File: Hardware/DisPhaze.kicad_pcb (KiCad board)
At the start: 2 copper layers, 71 x 24.1 mm, 13 parts, among them J1 Conn_01x27, J2 Conn_01x27, J3 Conn_01x04_Male, U1 STM32F405RGTx, Y1 Crystal

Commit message: Start PCB layout
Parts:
- added C10: 100nF, Capacitors_SMD:C_0805_HandSoldering, F.Cu at (137.0, 76.0)
- added C11: 100nF, Capacitors_SMD:C_0805_HandSoldering, F.Cu at (114.0, 65.0)
- added C12: 100nF, Capacitors_SMD:C_0805_HandSoldering, F.Cu at (149.0, 89.0)
- added C13: 1nF, Capacitors_SMD:C_0805_HandSoldering, F.Cu at (140.5, 100.5)
- added C14: 2.2nF, Capacitors_SMD:C_0805_HandSoldering, F.Cu at (137.2, 110.0)
- added C15: 2.2nF, Capacitors_SMD:C_0805_HandSoldering, F.Cu at (123.0, 98.8)
- added C16: 1nF, Capacitors_SMD:C_0805_HandSoldering, F.Cu at (121.5, 110.2)
- added C17: 10uF, Capacitors_SMD:C_0805_HandSoldering, F.Cu at (128.2, 79.0)
- added C18: 10uF, Capacitors_SMD:C_0805_HandSoldering, F.Cu at (130.8, 79.0)
- added C19: 18pF, Capacitors_SMD:C_0805_HandSoldering, F.Cu at (139.0, 90.0)
- added C20: 18pF, Capacitors_SMD:C_0805_HandSoldering, F.Cu at (124.5, 89.2)
- added C21: 47uF, Capacitors_SMD:CP_Elec_5x5.8, F.Cu at (146.0, 128.0)
- added C22: 22uF, Capacitors_SMD:CP_Elec_4x5.8, F.Cu at (146.0, 138.0)
- added C23: 22uF, Capacitors_SMD:CP_Elec_4x5.8, F.Cu at (136.5, 137.8)
- added C24: 100nF, Capacitors_SMD:C_0805_HandSoldering, F.Cu at (153.0, 96.0)
- added C25: 47uF, Capacitors_SMD:CP_Elec_5x5.8, F.Cu at (136.5, 128.0)
- added C9: 100nF, Capacitors_SMD:C_0805_HandSoldering, F.Cu at (125.0, 60.0)
- added CTune1: B10k, Potentiometers:Potentiometer_Alps_RK09K_Horizontal, B.Cu at (144.9, 117.0)
- added D1: LM4040DBZ-5, TO_SOT_Packages_SMD:SOT-23, F.Cu at (153.0, 100.0)
- added D2: 1N5819, Diodes_SMD:D_SOD-123, F.Cu at (122.0, 131.5)
- added D3: 1N5819, Diodes_SMD:D_SOD-123, F.Cu at (129.5, 135.2)
- added FTune1: B10k, Potentiometers:Potentiometer_Alps_RK09K_Horizontal, B.Cu at (110.0, 117.0)
- added J4: PD2_Amt_In, Custom_Footprints:THONKICONN_hole, B.Cu at (115.2, 152.0)
- added J5: VCA_In, Custom_Footprints:THONKICONN_hole, B.Cu at (125.0, 152.0)
- added J6: DAC1_Out, Custom_Footprints:THONKICONN_hole, B.Cu at (154.5, 152.0)
- added J7: DAC2_Out, Custom_Footprints:THONKICONN_hole, B.Cu at (105.5, 152.0)
- added J8: Eurorack_16_pin_power, Custom_Footprints:Eurorack_16_pin_header, F.Cu at (107.0, 125.0)
- added L1: L, Resistors_SMD:R_0805_HandSoldering, F.Cu at (144.0, 120.0)
- added PD1Amt1: B10k, Potentiometers:Potentiometer_Alps_RK09K_Horizontal, B.Cu at (145.0, 68.0)
- added PD1Type1: B10k, Potentiometers:Potentiometer_Alps_RK09K_Horizontal, B.Cu at (145.0, 92.0)
- added PD2Amt1: B10k, Potentiometers:Potentiometer_Alps_RK09K_Horizontal, B.Cu at (110.0, 68.0)
- added PD2Type1: B10k, Potentiometers:Potentiometer_Alps_RK09K_Horizontal, B.Cu at (110.0, 92.0)
- added R1: 47k, Resistors_SMD:R_0805_HandSoldering, F.Cu at (120.2, 148.5)
- added R10: 47k, Resistors_SMD:R_0805_HandSoldering, F.Cu at (138.0, 100.5)
- added R11: 56k, Resistors_SMD:R_0805_HandSoldering, F.Cu at (139.2, 110.0)
- added R12: 47k, Resistors_SMD:R_0805_HandSoldering, F.Cu at (123.0, 102.0)
- added R13: 47k, Resistors_SMD:R_0805_HandSoldering, F.Cu at (124.8, 110.2)
- added R14: 47k, Resistors_SMD:R_0805_HandSoldering, F.Cu at (143.2, 76.0)
- added R15: 47k, Resistors_SMD:R_0805_HandSoldering, F.Cu at (130.8, 84.2)
- added R16: 6.3k, Resistors_SMD:R_0805_HandSoldering, F.Cu at (137.0, 81.0)
- added R17: 680R, Resistors_SMD:R_0805_HandSoldering, F.Cu at (110.0, 141.0)
- added R18: 6.3k, Resistors_SMD:R_0805_HandSoldering, F.Cu at (128.2, 84.2)
- added R19: 68k, Resistors_SMD:R_0805_HandSoldering, F.Cu at (138.0, 84.0)
- added R2: 82k, Resistors_SMD:R_0805_HandSoldering, F.Cu at (147.2, 102.0)
- added R20: 68k, Resistors_SMD:R_0805_HandSoldering, F.Cu at (121.8, 89.2)
- added R21: 680R, Resistors_SMD:R_0805_HandSoldering, F.Cu at (154.0, 130.0)
- added R22: 680R, Resistors_SMD:R_0805_HandSoldering, F.Cu at (110.0, 143.8)
- added R23: 1k, Resistors_SMD:R_0805_HandSoldering, F.Cu at (140.0, 95.0)
- added R24: 1k, Resistors_SMD:R_0805_HandSoldering, F.Cu at (108.0, 100.0)
- added R25: 2.2k, Resistors_SMD:R_0805_HandSoldering, F.Cu at (130.8, 96.0)
- added R3: 100k, Resistors_SMD:R_0805_HandSoldering, F.Cu at (143.2, 100.5)
- added R4: 91k, Resistors_SMD:R_0805_HandSoldering, F.Cu at (146.0, 105.5)
- added R5: 100k, Resistors_SMD:R_0805_HandSoldering, F.Cu at (139.0, 115.0)
- added R6: 68k, Resistors_SMD:R_0805_HandSoldering, F.Cu at (117.2, 102.0)
- added R7: 100k, Resistors_SMD:R_0805_HandSoldering, F.Cu at (122.0, 143.0)
- added R8: 68k, Resistors_SMD:R_0805_HandSoldering, F.Cu at (123.0, 106.0)
- added R9: 100k, Resistors_SMD:R_0805_HandSoldering, F.Cu at (123.0, 115.0)
- added SW1: DAC1_RingMod_Switch, Custom_Footprints:SPDTSubMiniature, B.Cu at (154.0, 133.0)
- added SW2: DAC2_Mix_Switch, Custom_Footprints:SPDTSubMiniature, B.Cu at (105.8, 133.0)
- added SW3: Octave_Switch, Custom_Footprints:SPDTSubMiniature, B.Cu at (115.2, 133.0)
- added U2: MCP6004, SMD_Packages:SOIC-14_N, F.Cu at (131.0, 105.0)
- added U3: TL072, SMD_Packages:SOIC-8-N, F.Cu at (131.0, 90.0)
- added U4: LM1117-3.3, TO_SOT_Packages_SMD:SOT-223, F.Cu at (154.0, 125.0)
- C1: value 18pF -> 100nF
- C3: value 2.2uF -> 18pF
- C4: value 2.2uF -> 100nF; moved to F.Cu
- C5, C8: value 100nF -> 2.2uF; moved to F.Cu
- J1: value Conn_01x27 -> SWD_Header; footprint Custom_Footprints:Connector_27x2.54mm -> Custom_Footprints:4pin_header
- J2: value Conn_01x27 -> PItch_In; footprint Custom_Footprints:Connector_27x2.54mm -> Custom_Footprints:THONKICONN_hole; moved to B.Cu
- J3: value Conn_01x04_Male -> PD1_Amt_In; footprint Custom_Footprints:4pin_header -> Custom_Footprints:THONKICONN_hole; moved to B.Cu
- moved J2 74.8 mm to (134.8, 152.0)
- moved J1 72.3 mm to (127.0, 54.0)
- moved C3 68.9 mm to (121.0, 70.0), turned to 270 degrees
- moved C8 63.8 mm to (140.5, 64.8)
- moved J3 62.7 mm to (144.8, 152.0), turned to 180 degrees
- moved C2 58.5 mm to (121.0, 64.0)
- moved U1 55.8 mm to (130.0, 68.0), turned to 0 degrees
- moved C7 55.7 mm to (149.0, 65.0)
- moved C1 52.8 mm to (138.0, 61.0)
- moved C4 49.8 mm to (125.8, 79.0), turned to 270 degrees
- moved Y1 47.3 mm to (112.0, 74.0)
- moved C5 40.1 mm to (137.0, 78.5)
- moved C6 36.4 mm to (111.5, 114.0)
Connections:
- C1 pad 1: Net-(C1-Pad1) -> +3V3
- C3 pad 1: GND -> Net-(C3-Pad1)
- C3 pad 2: Net-(C3-Pad2) -> GND
- C4 pad 1: Net-(C4-Pad1) -> +3V3
- C5 pad 1: +3V3 -> GND
- C5 pad 2: GND -> Net-(C5-Pad2)
- C6 pad 1: +3V3 -> FTUNE
- C7 pad 1: +3V3 -> PD1_POT
- C8 pad 1: +3V3 -> Net-(C8-Pad1)
- J1 pad 2: p1 -> GND
- J1 pad 3: p2 -> SWDIO
- J1 pad 4: p3 -> SWCLK
- J2 pad 1: p34 -> GND
- J2 pad 2: p35 -> CV_IN
- J2 pad 3: p36 -> Net-(J2-Pad3)
- J3 pad 1: +3V3 -> GND
- J3 pad 3: SWDIO -> Net-(J3-Pad3)
- U1 pad 1: p1 -> Net-(U1-Pad1)
- U1 pad 10: p10 -> PD1_CV
- U1 pad 11: p11 -> Net-(U1-Pad11)
- U1 pad 13: p13 -> +3.3VA
- U1 pad 14: p14 -> Net-(U1-Pad14)
- U1 pad 15: p15 -> PD1_TYPE
- U1 pad 16: p16 -> PD2_TYPE
- U1 pad 17: p17 -> PD2_CV
- U1 pad 2: p2 -> Net-(U1-Pad2)
- U1 pad 20: p20 -> DAC1_OUT
- U1 pad 21: p21 -> DAC2_OUT
- U1 pad 22: p22 -> Net-(U1-Pad22)
- U1 pad 23: p23 -> PD1_POT
- U1 pad 24: p24 -> FTUNE
- U1 pad 25: p25 -> Net-(U1-Pad25)
- U1 pad 26: p26 -> V_OCT_CV
- U1 pad 27: p27 -> CTUNE
- U1 pad 28: p28 -> Net-(U1-Pad28)
- U1 pad 29: p29 -> Net-(U1-Pad29)
- U1 pad 3: p3 -> Net-(U1-Pad3)
- U1 pad 30: p30 -> Net-(U1-Pad30)
- U1 pad 31: Net-(C3-Pad2) -> Net-(C5-Pad2)
- U1 pad 33: p33 -> OCTAVE_UP
- U1 pad 34: p34 -> OCTAVE_DN
- U1 pad 35: p35 -> Net-(U1-Pad35)
- U1 pad 36: p36 -> Net-(U1-Pad36)
- U1 pad 37: p37 -> DAC1_RING_MOD
- U1 pad 38: p38 -> Net-(U1-Pad38)
- U1 pad 39: p39 -> Net-(U1-Pad39)
- U1 pad 4: p4 -> Net-(U1-Pad4)
- U1 pad 40: p40 -> Net-(U1-Pad40)
- U1 pad 41: p41 -> Net-(U1-Pad41)
- U1 pad 42: p42 -> Net-(U1-Pad42)
- U1 pad 43: p43 -> Net-(U1-Pad43)
- U1 pad 44: p44 -> Net-(U1-Pad44)
- U1 pad 45: p45 -> Net-(U1-Pad45)
- U1 pad 47: Net-(C4-Pad1) -> Net-(C8-Pad1)
- U1 pad 5: Net-(C1-Pad1) -> Net-(C2-Pad1)
- U1 pad 50: p50 -> Net-(U1-Pad50)
- U1 pad 51: p51 -> Net-(U1-Pad51)
- U1 pad 52: p52 -> Net-(U1-Pad52)
- U1 pad 53: p53 -> Net-(U1-Pad53)
- U1 pad 54: p54 -> Net-(U1-Pad54)
- U1 pad 55: p55 -> Net-(U1-Pad55)
- U1 pad 56: p56 -> Net-(U1-Pad56)
- U1 pad 57: p57 -> Net-(U1-Pad57)
- U1 pad 58: p58 -> Net-(U1-Pad58)
- U1 pad 59: p59 -> Net-(U1-Pad59)
- U1 pad 6: Net-(C2-Pad1) -> Net-(C3-Pad1)
- U1 pad 60: p60 -> Net-(U1-Pad60)
- U1 pad 61: p61 -> DAC2_MIX
- U1 pad 62: p62 -> Net-(U1-Pad62)
- U1 pad 7: p7 -> Net-(U1-Pad7)
- U1 pad 8: p8 -> VCA
- U1 pad 9: p9 -> PD2_POT
- Y1 pad 1: Net-(C2-Pad1) -> Net-(C3-Pad1)
- Y1 pad 2: Net-(C1-Pad1) -> Net-(C2-Pad1)
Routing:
- net +3.3VA: track 0.00 -> 166.9 mm, vias 0 -> 3
- net DAC2_MIX: track 0.00 -> 111.3 mm
- net DAC1_RING_MOD: track 0.00 -> 91.5 mm, vias 0 -> 1
- net FTUNE: track 0.00 -> 66.9 mm, vias 0 -> 1
- net AREF_-5: track 0.00 -> 60.4 mm
- net VCA: track 0.00 -> 56.1 mm, vias 0 -> 2
- net CTUNE: track 0.00 -> 53.5 mm, vias 0 -> 1
- net Net-(J7-Pad3): track 0.00 -> 49.8 mm, vias 0 -> 1
- net PD1_TYPE: track 0.00 -> 46.3 mm, vias 0 -> 1
- net V_OCT_CV: track 0.00 -> 36.9 mm, vias 0 -> 2
- net p33: track 34.8 -> 0.00 mm
- net SWCLK: track 42.9 -> 8.66 mm, vias 1 -> 0
- net Net-(J5-Pad3): track 0.00 -> 33.7 mm
- net PD2_CV: track 0.00 -> 33.3 mm, vias 0 -> 2
- net p34: track 33.2 -> 0.00 mm
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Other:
- board size 71 x 24.1 mm -> 60 x 110 mm
- rule pad_to_mask_clearance: 0.051 -> 0
- board text removed: "1"
- board text removed: "10"
- board text removed: "11"
- board text removed: "13"
- board text removed: "14"
- board text removed: "15"
- board text removed: "16"
- board text removed: "17"
- board text removed: "2"
- board text removed: "20"
- board text removed: "21"
- board text removed: "22"
- board text removed: "23"
- board text removed: "24"
- board text removed: "25"
- board text removed: "26"
- board text removed: "27"
- board text removed: "28"
- board text removed: "29"
- board text removed: "3"
- board text removed: "30"
- board text removed: "33"
- board text removed: "34"
- board text removed: "35"
- board text removed: "36"
- board text removed: "37"
- board text removed: "38"
- board text removed: "39"
- board text removed: "3V3"
- board text removed: "4"
- board text removed: "40"
- board text removed: "41"
- board text removed: "42"
- board text removed: "43"
- board text removed: "44"
- board text removed: "45"
- board text removed: "50"
- board text removed: "51"
- board text removed: "52"
- board text removed: "53"
- board text removed: "54"
- board text removed: "55"
- board text removed: "56"
- board text removed: "57"
- board text removed: "58"
- board text removed: "59"
- board text removed: "60"
- board text removed: "61"
- board text removed: "62"
- board text removed: "7"
- board text removed: "8"
- board text removed: "9"
- board text removed: "DisPhaze V2"
- board text removed: "G"
- board text removed: "SWCLK"
- board text removed: "SWDIO"

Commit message: First schematic draft
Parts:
- moved C22 30.9 mm to (119.2, 122.5)
- moved C23 27.3 mm to (113.2, 123.5)
- moved J8 22.2 mm to (125.5, 137.2)
- moved C21 21.4 mm to (125.5, 121.8), turned to 270 degrees
- moved U4 20.3 mm to (133.8, 124.0), turned to 270 degrees
- moved D2 18.2 mm to (139.5, 126.5), turned to 270 degrees
- moved C25 15.7 mm to (151.5, 123.2), turned to 0 degrees
- moved R17 14.4 mm to (117.5, 128.8)
- moved R25 12.8 mm to (118.2, 98.8), turned to 270 degrees
- moved R14 12.8 mm to (133.5, 84.2), turned to 270 degrees
- moved R1 12.4 mm to (131.5, 143.2), turned to 180 degrees
- moved D3 9.10 mm to (124.0, 128.0), turned to 180 degrees
- moved R7 6.54 mm to (115.5, 143.8), turned to 180 degrees
- moved SW3 5.00 mm to (115.2, 138.0), turned to 90 degrees
- moved R22 2.53 mm to (110.4, 141.2)
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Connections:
- U1 pad 33: OCTAVE_UP -> Net-(U1-Pad33)
- U1 pad 34: OCTAVE_DN -> Net-(U1-Pad34)
- U1 pad 51: Net-(U1-Pad51) -> OCTAVE_UP
- U1 pad 53: Net-(U1-Pad53) -> OCTAVE_DN
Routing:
- net +3V3: track 98.2 -> 212.1 mm, vias 1 -> 8
- net OCTAVE_UP: track 0.00 -> 102.8 mm, vias 0 -> 1
- net OCTAVE_DN: track 0.00 -> 101.7 mm
- net Net-(J6-Pad3): track 0.00 -> 67.7 mm
- net Net-(J2-Pad3): track 0.00 -> 67.4 mm, vias 0 -> 1
- net VCC: track 12.5 -> 76.0 mm, vias 0 -> 2
- net PD1_CV: track 6.30 -> 69.1 mm, vias 0 -> 2
- net VEE: track 8.95 -> 63.0 mm
- net Net-(C15-Pad1): track 13.3 -> 56.3 mm, vias 0 -> 2
- net Net-(J3-Pad3): track 0.00 -> 33.1 mm, vias 0 -> 1
- net CV_IN: track 0.00 -> 23.6 mm
- net DAC2_MIX: track 111.3 -> 99.6 mm
- net GND: track 0.00 -> 11.6 mm, vias 0 -> 9
- net +12V: track 0.00 -> 10.7 mm
- net -12V: track 0.00 -> 9.31 mm
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
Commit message: Tweaks to pcb layout v1
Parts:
- moved C19 1.50 mm to (139.0, 88.5), turned to 90 degrees
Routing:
- net DAC1_RING_MOD: track 89.3 -> 80.8 mm
- net Net-(C19-Pad1): track 14.0 -> 16.2 mm
- net CTUNE: track 51.1 -> 51.7 mm

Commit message: rev2 branch test
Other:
- board text added: "DisPhaze v2"
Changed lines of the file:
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@@
   (general
     (thickness 1.6)
-    (drawings 4)
+    (drawings 5)
     (tracks 512)
     (zones 0)
@@
     )
   )
+  (gr_text "DisPhaze v2" (at 148.75 52.5) (layer F.Cu)
+    (effects (font (size 1.5 1.5) (thickness 0.3)))
+  )
   (gr_line (start 160 50) (end 160 160) (layer Edge.Cuts) (width 0.2))

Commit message: rev2 pcb layout
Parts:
- moved C9 1.27 mm to (124.5, 59.2), turned to 180 degrees
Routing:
- net PD1_CV: track 69.1 -> 104.5 mm
- net +3V3: track 212.1 -> 178.2 mm, vias 8 -> 4
- net +3.3VA: track 168.4 -> 150.8 mm
- net FTUNE: track 67.2 -> 56.2 mm
- net OCTAVE_UP: track 102.8 -> 111.4 mm
- net PD1_TYPE: track 46.8 -> 38.3 mm
- net DAC2_MIX: track 99.6 -> 107.5 mm, vias 0 -> 1
- net DAC1_RING_MOD: track 80.8 -> 88.1 mm, vias 1 -> 0
- net GND: track 11.6 -> 18.3 mm, vias 9 -> 5
- net Net-(J6-Pad3): track 67.7 -> 61.2 mm, vias 0 -> 1
- net V_OCT_CV: track 36.9 -> 39.5 mm
- net Net-(J5-Pad3): track 34.2 -> 31.9 mm
- net Net-(J2-Pad3): track 67.4 -> 65.2 mm
- net PD2_CV: track 35.0 -> 33.1 mm
- net VEE: track 63.0 -> 64.7 mm
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
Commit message: rev2 layout completed
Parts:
- J1: footprint Custom_Footprints:4pin_header -> Custom_Footprints:SWD_header
- U4: footprint TO_SOT_Packages_SMD:SOT-223 -> TO_SOT_Packages_SMD:TO-252-3_TabPin2
- moved D2 11.2 mm to (128.5, 128.5)
- moved R1 2.70 mm to (128.8, 143.3), turned to 0 degrees
- moved R22 1.03 mm to (110.8, 140.3), turned to 90 degrees
- moved C9 0.50 mm to (124.0, 59.2)
- moved U4 0.40 mm to (133.8, 123.6)
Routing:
- net +3V3: track 178.2 -> 189.7 mm
- net GND: track 18.3 -> 10.2 mm, vias 5 -> 6
- net VCC: track 74.9 -> 68.1 mm
- net DAC1_RING_MOD: track 88.1 -> 93.7 mm
- net PD1_CV: track 104.5 -> 107.9 mm
- net VEE: track 64.7 -> 61.5 mm
- net +3.3VA: track 150.8 -> 152.3 mm
- net OCTAVE_DN: track 100.6 -> 101.9 mm
- net +12V: track 10.7 -> 11.8 mm
- net Net-(R22-Pad2): track 9.91 -> 9.12 mm
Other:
- net class Wide_Power added: clearance 0.2, trace_width 0.5, via_dia 0.8, via_drill 0.4

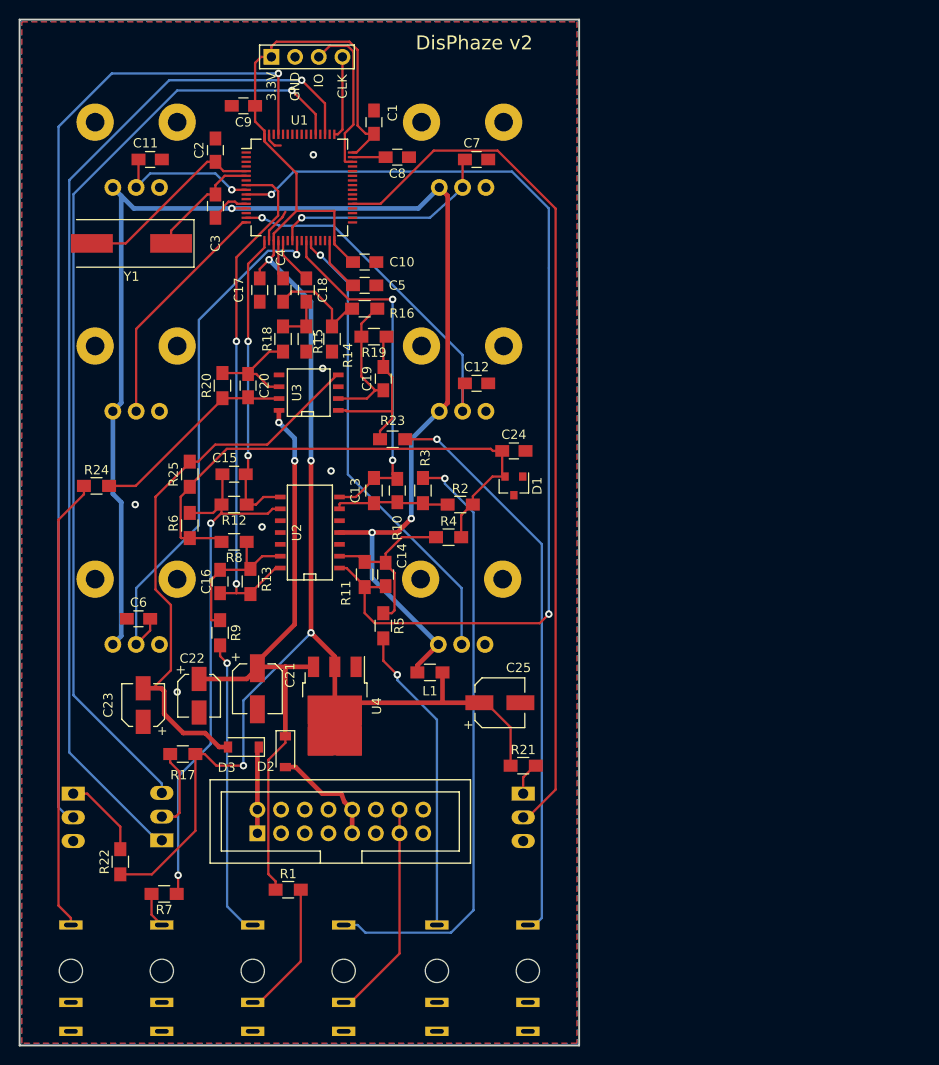
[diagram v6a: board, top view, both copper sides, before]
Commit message: Updated schematic silk screen
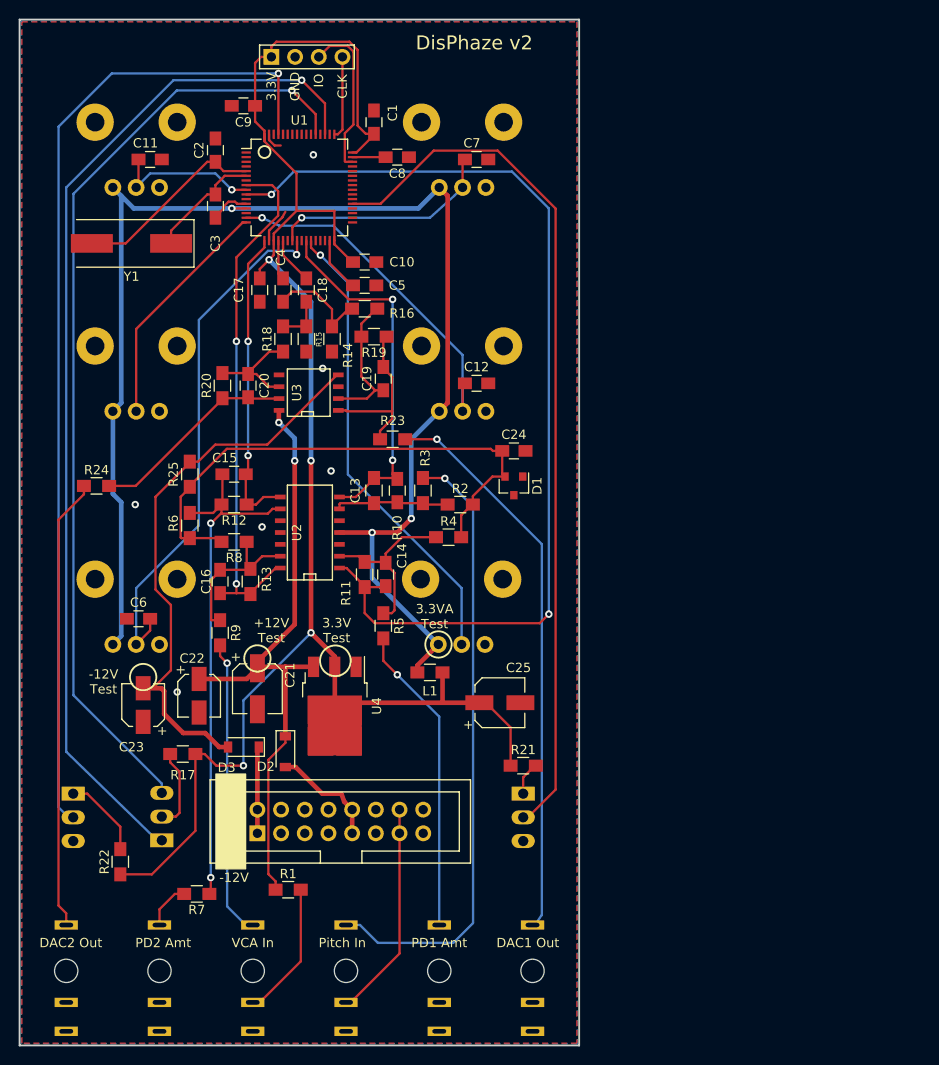
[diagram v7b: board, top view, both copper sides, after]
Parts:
- moved R7 3.50 mm to (119.0, 143.8)
- moved J6 0.50 mm to (155.0, 152.0)
- moved J7 0.50 mm to (105.0, 152.0)
- moved J2 0.25 mm to (135.0, 152.0)
- moved J3 0.25 mm to (145.0, 152.0)
- moved J4 0.25 mm to (115.0, 152.0)
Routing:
- net Net-(C15-Pad1): track 57.4 -> 55.9 mm
- net Net-(J2-Pad3): track 65.2 -> 66.6 mm
- net Net-(J4-Pad3): track 3.79 -> 5.01 mm
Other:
- board text added: "+12V Test"
- board text added: "-12V Test"
- board text added: "3.3V Test"
- board text added: "3.3VA Test"
- board text added: "DAC1 Out"
- board text added: "DAC2 Out"
- board text added: "Mix"
- board text added: "Octave"
- board text added: "PD1 Amt"
- board text added: "PD2 Amt"
- board text added: "Pitch In"
- board text added: "Ring Mod"
- board text added: "VCA In"

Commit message: Panel outline first draft
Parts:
- moved SW3 5.00 mm to (115.2, 133.0), turned to 270 degrees
- moved R21 4.27 mm to (150.0, 128.5), turned to 180 degrees
- moved SW1 4.00 mm to (150.0, 133.0)
- moved J8 0.25 mm to (125.2, 137.2)
- moved CTune1 0.10 mm to (145.0, 117.0)
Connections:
- SW3 pad 1: OCTAVE_UP -> OCTAVE_DN
- SW3 pad 3: OCTAVE_DN -> OCTAVE_UP
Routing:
- net Net-(J2-Pad3): track 66.6 -> 71.8 mm
- net DAC1_RING_MOD: track 93.7 -> 97.7 mm
- net +3V3: track 189.7 -> 187.6 mm
- net Net-(R21-Pad2): track 3.62 -> 5.12 mm
